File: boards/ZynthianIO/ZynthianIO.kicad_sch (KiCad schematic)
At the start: 32 parts, among them J1 Btn-1, J10 Ctrl-2, J11 Display, J2 Raspberry_Pi_2_3, J3 Btn-2, J7 Ctrl-3, J8 Ctrl-4, J9 Ctrl-1, U1 MCP23017_SP, U2 74LS07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

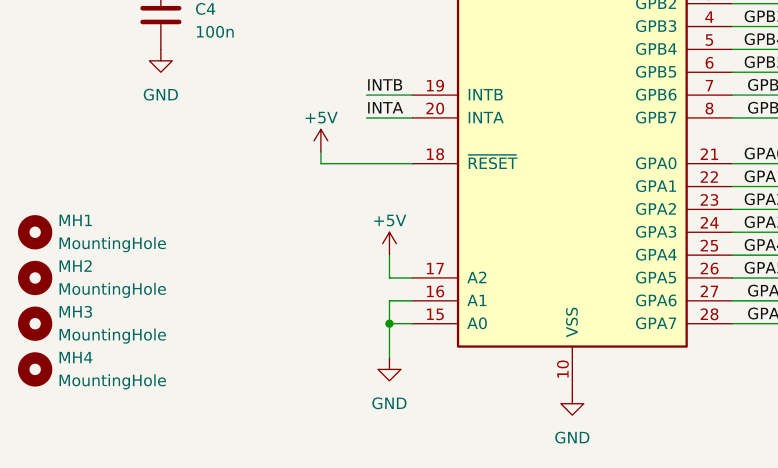
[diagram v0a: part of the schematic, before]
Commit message: Fixed ground plane connection, change 23017 address from 0x24 to 0x21
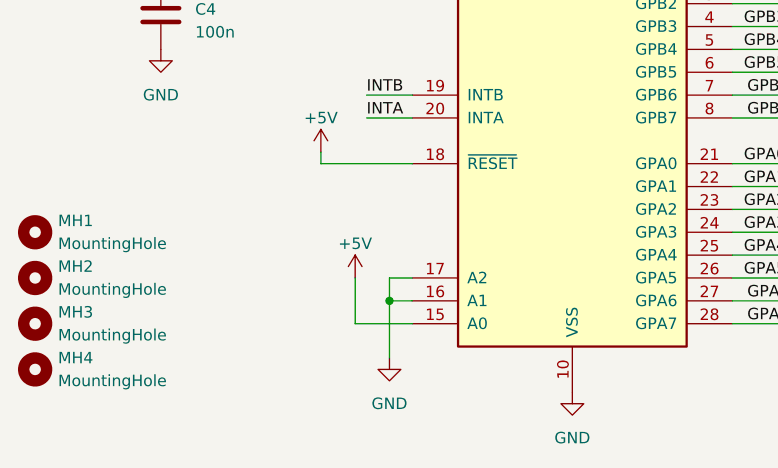
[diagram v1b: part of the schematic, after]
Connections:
- net +5V: now also U1.15 (A0); no longer U1.17 (A2)
- net GND: now also U1.17 (A2); no longer U1.15 (A0)
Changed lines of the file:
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@@
+	)
+	(junction
+		(at 62.23 177.8)
+		(diameter 0)
+		(color 0 0 0 0)
 	)
 	(junction
@@
 	)
 	(junction
-		(at 62.23 180.34)
-		(diameter 0)
-		(color 0 0 0 0)
-	)
-	(junction
 		(at 186.69 33.02)
 		(diameter 0)
@@
 	(wire
 		(pts
+			(xy 64.77 180.34) (xy 58.42 180.34)
+		)
+		(stroke
+			(width 0)
+			(type default)
+		)
+	)
+	(wire
+		(pts
 			(xy 166.37 158.75) (xy 167.64 158.75)
 		)
@@
 	(wire
 		(pts
-			(xy 62.23 180.34) (xy 62.23 184.15)
+			(xy 62.23 177.8) (xy 62.23 184.15)
 		)
 		(stroke
@@
 	(wire
 		(pts
+			(xy 58.42 180.34) (xy 58.42 175.26)
+		)
+		(stroke
+			(width 0)
+			(type default)
+		)
+	)
+	(wire
+		(pts
 			(xy 217.17 80.01) (xy 223.52 80.01)
 		)
@@
 	(wire
 		(pts
-			(xy 62.23 180.34) (xy 64.77 180.34)
-		)
-		(stroke
-			(width 0)
-			(type default)
-		)
-	)
-	(wire
-		(pts
 			(xy 256.54 105.41) (xy 252.73 105.41)
 		)
@@
 	(wire
 		(pts
-			(xy 62.23 172.72) (xy 62.23 175.26)
-		)
-		(stroke
-			(width 0)
-			(type default)
-		)
-	)
-	(wire
-		(pts
 			(xy 46.99 57.15) (xy 58.42 57.15)
 		)
@@
 	(wire
 		(pts
-			(xy 62.23 177.8) (xy 62.23 180.34)
-		)
-		(stroke
-			(width 0)
-			(type default)
-		)
-	)
-	(wire
-		(pts
 			(xy 210.82 102.87) (xy 223.52 102.87)
 		)
@@
 		(pts
 			(xy 167.64 179.07) (xy 166.37 179.07)
+		)
+		(stroke
+			(width 0)
+			(type default)
+		)
+	)
+	(wire
+		(pts
+			(xy 62.23 175.26) (xy 62.23 177.8)
 		)
 		(stroke
@@
 	(symbol
 		(lib_id "power:+5V")
-		(at 62.23 172.72 0)
+		(at 58.42 175.26 0)
 		(unit 1)
 		(exclude_from_sim no)
@@
 		(fields_autoplaced yes)
 		(property "Reference" "#PWR011"
-			(at 62.23 176.53 0)
+			(at 58.42 179.07 0)
 			(effects
 				(font
@@
 		)
 		(property "Value" "+5V"
-			(at 62.23 168.91 0)
+			(at 58.42 171.45 0)
 			(effects
 				(font
@@
 		)
 		(property "Footprint" ""
-			(at 62.23 172.72 0)
+			(at 58.42 175.26 0)
 			(effects
 				(font
@@
 		)
 		(property "Datasheet" ""
-			(at 62.23 172.72 0)
+			(at 58.42 175.26 0)
 			(effects
 				(font
@@
 		)
 		(property "Description" "Power symbol creates a global label with name \"+5V\""
-			(at 62.23 172.72 0)
-			(effects
-				(font
+			(at 58.42 175.26 0)
+			(effects
+				(font
